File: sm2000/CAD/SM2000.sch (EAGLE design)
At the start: 228 parts, among them CN1 HDR100-3, CN10 ST-3509, CN11 HDR100-3, CN2 JS-MU3-002, CN3 DS-0518, CN5 ST-3509, CN8 ST-3509, J1 JMP-2PIN, J2 JMP-2PIN, J3 JMP-2PIN, J4 CONN-BOOM-XH-2A, P10 TPAD50, P11 TPAD50, P12 TPAD50, P13 TPAD50, P14 TPAD50, P16 TPAD50, P18 TPAD50, P19 TPAD50, P20 TPAD50, P21 TPAD50, P3 TPAD50, P4 TPAD50, P5 TPAD50, P6 TPAD50, P7 TPAD50, P8 TPAD50, P9 TPAD50, Q1 MMBT3904, Q2 MMBT3904, Q3 MMBT3904, Q4 MMBT3904, Q5 MMBT3904, Q6 MMBT3904, Q7 BC548, Q8 BC549, SW1 SW-LC2259, SW2 TS-026, SW3 SW-LC2259EENP, SW4 TS-026, SW5 TS-02B, U1 STM32F405VGT6, U10 DNL, U2 LD3985M33R, U3 STMPS2141, U4 EMIF02-USB03F2, U5 TPS54329E, U8 LM386M-1, U9 LMV341, X1 BU-SMA-H, X2 BU-SMA-H

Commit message: Continued edit of SM2000 .sch & .brd   RGB
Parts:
- removed R55: 0 Ohm, AA-ipc-7351-resistor:RESISTOR_0603
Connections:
- removed net !CPPT!: U1A.PD10
- removed net DAC1_OUT: R55.2
- removed net N$11: R55.1, U1A.PA4
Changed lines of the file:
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@@
 <part name="V124" library="A-SUPPLY2" deviceset="GND" device=""/>
 <part name="FB7" library="_RoweTel" deviceset="FB0805" device=""/>
-<part name="R55" library="AA-ipc-7351-resistor" deviceset="RESISTOR_" device="0603" value="0 Ohm"/>
 <part name="R54" library="AA-ipc-7351-resistor" deviceset="RESISTOR_" device="0603" value="0 Ohm"/>
 <part name="C55" library="AA-ipc-7351-capacitor" deviceset="CAPACITOR_" device="0402" value="1nF,25V,0402"/>
@@
 <instance part="V124" gate="GND" x="43.18" y="106.68"/>
 <instance part="FB7" gate="G$1" x="20.32" y="60.96"/>
-<instance part="R55" gate="G$1" x="83.82" y="208.28" smashed="yes" rot="R180">
-<attribute name="NAME" x="81.28" y="210.82" size="1.4224" layer="95" ratio="9"/>
-<attribute name="VALUE" x="86.36" y="210.82" size="1.4224" layer="96" ratio="9"/>
-</instance>
 <instance part="R54" gate="G$1" x="83.82" y="203.2" smashed="yes" rot="R180">
 <attribute name="NAME" x="81.788" y="204.978" size="1.4224" layer="95" ratio="9"/>
@@
 </segment>
 </net>
-<net name="!CPPT!" class="0">
-<segment>
-<pinref part="U1" gate="A" pin="PD10"/>
-<wire x1="147.32" y1="149.86" x2="165.1" y2="149.86" width="0.1524" layer="91"/>
-<label x="149.86" y="150.368" size="1.4224" layer="95" ratio="10"/>
-</segment>
-</net>
 <net name="!TEST!" class="0">
 <segment>
@@
 </segment>
 </net>
-<net name="DAC1_OUT" class="0">
-<segment>
-<pinref part="R55" gate="G$1" pin="2"/>
-<wire x1="78.74" y1="208.28" x2="66.04" y2="208.28" width="0.1524" layer="91"/>
-<label x="68.58" y="208.788" size="1.4224" layer="95" ratio="10"/>
-</segment>
-</net>
 <net name="DAC2_OUT" class="0">
 <segment>
@@
 </segment>
 </net>
-<net name="N$11" class="0">
-<segment>
-<pinref part="R55" gate="G$1" pin="1"/>
-<pinref part="U1" gate="A" pin="PA4"/>
-<wire x1="88.9" y1="208.28" x2="111.76" y2="208.28" width="0.1524" layer="91"/>
-</segment>
-</net>
 <net name="N$13" class="0">
 <segment>
@@
 <net name="N$90" class="0">
 <segment>
-<pinref part="C69" gate="G$1" pin="1"/>
-<wire x1="132.08" y1="215.9" x2="134.62" y2="215.9" width="0.1524" layer="91"/>
 <pinref part="C76" gate="G$1" pin="2"/>
-<wire x1="134.62" y1="215.9" x2="137.16" y2="215.9" width="0.1524" layer="91"/>
 <wire x1="134.62" y1="152.4" x2="137.16" y2="152.4" width="0.1524" layer="91"/>
-<wire x1="134.62" y1="215.9" x2="137.16" y2="215.9" width="0.1524" layer="91"/>
 <wire x1="137.16" y1="215.9" x2="137.16" y2="152.4" width="0.1524" layer="91"/>
 <pinref part="X2" gate="G$1" pin="1"/>
 <wire x1="144.78" y1="215.9" x2="137.16" y2="215.9" width="0.1524" layer="91"/>
+<pinref part="C69" gate="G$1" pin="1"/>
+<wire x1="137.16" y1="215.9" x2="134.62" y2="215.9" width="0.1524" layer="91"/>
+<wire x1="132.08" y1="215.9" x2="134.62" y2="215.9" width="0.1524" layer="91"/>
 <junction x="137.16" y="215.9"/>
 </segment>

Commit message: MERGE SCHEMATICS INTO sm2000.SCH AND UPDATE LIBRARY rgb
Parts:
- added C100, C93: 33p, rcl:C-EU025-024X044
- added C118, C121, C124, C125, C126, C129, C131, C91, C92, C97: 0.1u, rcl:C-EU025-024X044
- added C119: 10uF, _RoweTel:CAP-1210
- added C120: 39pF, rcl:C-EU025-024X044
- added C122, C89: 5p6, rcl:C-EU025-024X044
- added C123: 2-12pF, c-trimm:C-TRIMM3008
- added C127: 27pF, rcl:C-EU025-024X044
- added C128, C132: 150pF, rcl:C-EU025-024X044
- added C130, C133, C134, C88, C90, C96, C98: 1n, rcl:C-EU025-024X044
- added C87: 22pF, AA-ipc-7351-capacitor:CAPACITOR_0805
- added C94: 22p, rcl:C-EU025-024X044
- added C95: 1n DNL, rcl:C-EU025-024X044
- added C99: 47p, rcl:C-EU025-024X044
- added FB11, FB14, FB15, FB6: FB0805, _RoweTel:FB0805
- added L10: 168nH, rcl:L-US0204/5
- added L11, L13: RFC, inductor-neosid:Z14/40CCW
- added L12: 54nH, rcl:L-US0204/5
- added L14, L15: 57nH air core 4T 2mm ID, rcl:L-US0204/5
- added L20: 5.7uH +/- 10% Q>20, rcl:L-US0204/5
- added L21: 9.2uH +/- 10% Q>20, rcl:L-US0204/5
- added L22: 5.2uH +/- 10% Q>20, rcl:L-US0204/5
- added L23: 15uH +/- 10% Q>20, rcl:L-US0204/5
- added L9: 57nH, rcl:L-US0204/5
- added Q12: BRF92, transistor:-NPN-SOT23-EBC
- added Q13: BFQ19, transistor:-NPN-SOT23-EBC
- added Q14: RD01MUS2, _RoweTel:RD01MUS2
- added Q17, Q18: MMT2904, transistor:-NPN-SOT23-EBC
- added R108, R60, R93: 3k, AA-ipc-7351-resistor:RESISTOR_0805
- added R109, R113, R94: 1k, AA-ipc-7351-resistor:RESISTOR_0805
- added R110, R96, R97: 10, AA-ipc-7351-resistor:RESISTOR_0805
- added R111: 33k, AA-ipc-7351-resistor:RESISTOR_0805
- added R112: 15k, AA-ipc-7351-resistor:RESISTOR_0805
- added R114, R95: 50, AA-ipc-7351-resistor:RESISTOR_0805
- added R115, R92: 150, AA-ipc-7351-resistor:RESISTOR_0805
- added R55: 10k, AA-ipc-7351-resistor:RESISTOR_0805
- added R98: 47 DNL, AA-ipc-7351-resistor:RESISTOR_0805
- added R99: 4k7, AA-ipc-7351-resistor:RESISTOR_0805
- added U$10, U$11: ECS-10.7-15B, _RoweTel:ECS-10.7-15B
- added U7: SA612A, _RoweTel:SA612A
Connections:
- new net N$11: C100.1, L14.2
- new net N$112: C87.2, L9.1
- new net N$113: C95.1, R98.1
- new net N$114: C96.1, FB11.1, R99.2
- new net N$115: C97.1, FB6.2, R99.1
- new net N$116: L13.1
- new net N$118: C93.1, C98.2, L15.1
- new net N$140: C118.1, Q17.C, R108.2, R110.2, R111.2
- new net N$141: C121.2, Q17.B, Q18.C, R108.1
- new net N$142: C119.1, FB14.1, R110.1
- new net N$143: C120.1, L20.2, U$11.1
- new net N$144: C122.1, U$10.2, U$11.2
- new net N$145: C121.1, C123.E, L21.2, U$10.1
- new net N$146: C124.1, Q18.B, R111.1, R112.2
- new net N$147: C125.1, Q18.E, R113.2
- new net N$148: C126.1, Q17.E, R109.2
- new net N$149: C126.2, C127.1, C128.2, R114.2
- new net N$150: C128.1, C129.2, L22.2, U7.IN_B
- new net N$151: C127.2, L22.1, U7.IN_A
- new net N$152: FB15.2, R115.2
- new net N$153: C130.2, C131.2, R115.1, U7.VIN
- new net N$154: C132.2, U7.OSC_B
- new net N$155: C132.1
- new net N$156: C133.2, L23.1, U7.OUT_A
- new net N$157: C134.2, L23.2
- new net N$32: C98.1, L11.1, Q14.D
- new net N$33: C94.1, FB11.2, Q14.G, R98.2
- new net N$70: C88.1, Q12.E, R92.2
- new net N$71: C90.1, Q13.E, R95.2
- new net N$73: C91.1, L10.1, R55.2, R96.2
- new net N$74: C92.1, L12.1, R93.2, R96.1, R97.2
- new net N$75: C89.1, Q13.B, R93.1, R94.2
- new net N$78: C87.1, Q12.B, R55.1, R60.2
- new net N$79: L11.2, L13.2, R97.1
- new net N$82: C89.2, L10.2, Q12.C
- new net N$84: C94.2, L12.2, Q13.C
- new net N$9: C99.1, L14.1, L15.2
- new net VGG: FB6.1
- net +12V: now also FB14.2, FB15.1
- net GND: now also C100.2, C118.2, C119.2, C120.2, C122.2, C123.A, C129.1, C131.1, C133.1, C134.1, C88.2, C90.2, C91.2, C92.2, C93.2, C95.2, C96.2, C97.2, C99.2, L21.1, L9.2, Q14.S, R109.1, R113.1, R114.1, R60.1, R92.1, R94.1, R95.1, U7.GND
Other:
- note added: "+9V"
- note added: "1.4V"
- note added: "1.7V"
- note added: "2.4V"
- note added: "33p, 47p, 33p cap nets must be zero length"
- note added: "3T 6.25mm"
- note added: "6T 6.25mm"
- note added: "BASEBAND_AMP"
- note added: "Baseand AMP"
- note added: "DRIVER_PA"
- note added: "From TIA"
- note added: "Load/Adjust if PA stability is a problem"
- note added: "Mount Ls at right angles"
- note added: "No junction here!"
- note added: "TERMINATION INSENSATIVE AMPLIFIEER"
- note added: "TX 2ND LO"
- note added: "TX DAC"
- note added: "Vgg from uC DAC"
- note added: "XTAL 2ND MIXER"
- note added: "Z=1500"
- note added: "Z=3000"
- note added: "Z=50"
- note added: "from BPF/switch"
- note added: "to T/R switch"
- moved on the sheet: C28, C67, C68, C69, C71, C72, C73, C74, C75, C76, C77, C78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

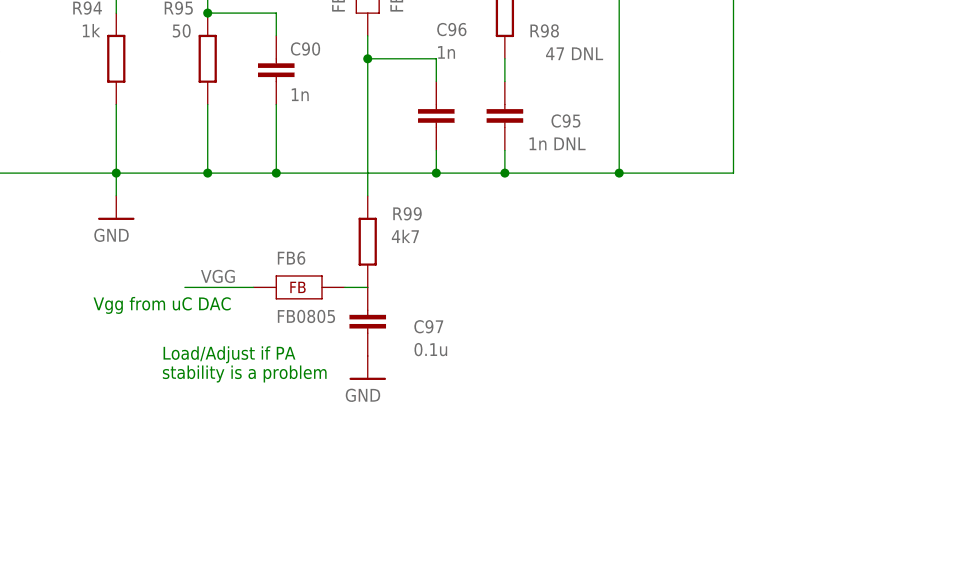
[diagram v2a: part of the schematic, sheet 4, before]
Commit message: test tweak by DR to sm2000.sch
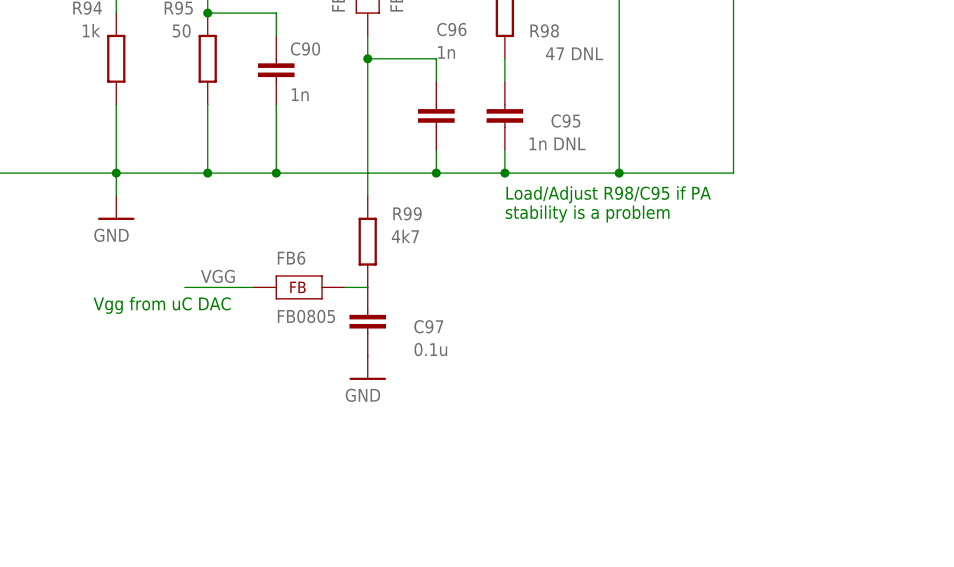
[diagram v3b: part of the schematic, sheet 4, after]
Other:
- note added: "Load/Adjust R98/C95 if PA stability is a problem"
- note removed: "Load/Adjust if PA stability is a problem"
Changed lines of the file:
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@@
 <?xml version="1.0" encoding="utf-8"?>
 <!DOCTYPE eagle SYSTEM "eagle.dtd">
-<eagle version="6.5.0">
+<eagle version="7.2.0">
 <drawing>
 <settings>
@@
 <setting verticaltext="up"/>
 </settings>
-<grid distance="0.1" unitdist="inch" unit="inch" style="lines" multiple="1" display="yes" altdistance="0.01" altunitdist="inch" altunit="inch"/>
+<grid distance="0.1" unitdist="inch" unit="inch" style="lines" multiple="1" display="no" altdistance="0.01" altunitdist="inch" altunit="inch"/>
 <layers>
 <layer number="1" name="Top" color="4" fill="1" visible="no" active="no"/>
@@
 <text x="88.9" y="43.18" size="1.4224" layer="91">Vgg from uC DAC</text>
 <text x="160.02" y="121.92" size="1.4224" layer="91">+9V</text>
-<text x="96.52" y="35.56" size="1.4224" layer="91">Load/Adjust if PA
+<text x="134.62" y="53.34" size="1.4224" layer="91">Load/Adjust R98/C95 if PA
 stability is a problem</text>
 <text x="33.02" y="88.9" size="1.4224" layer="91" rot="R180">from BPF/switch</text>

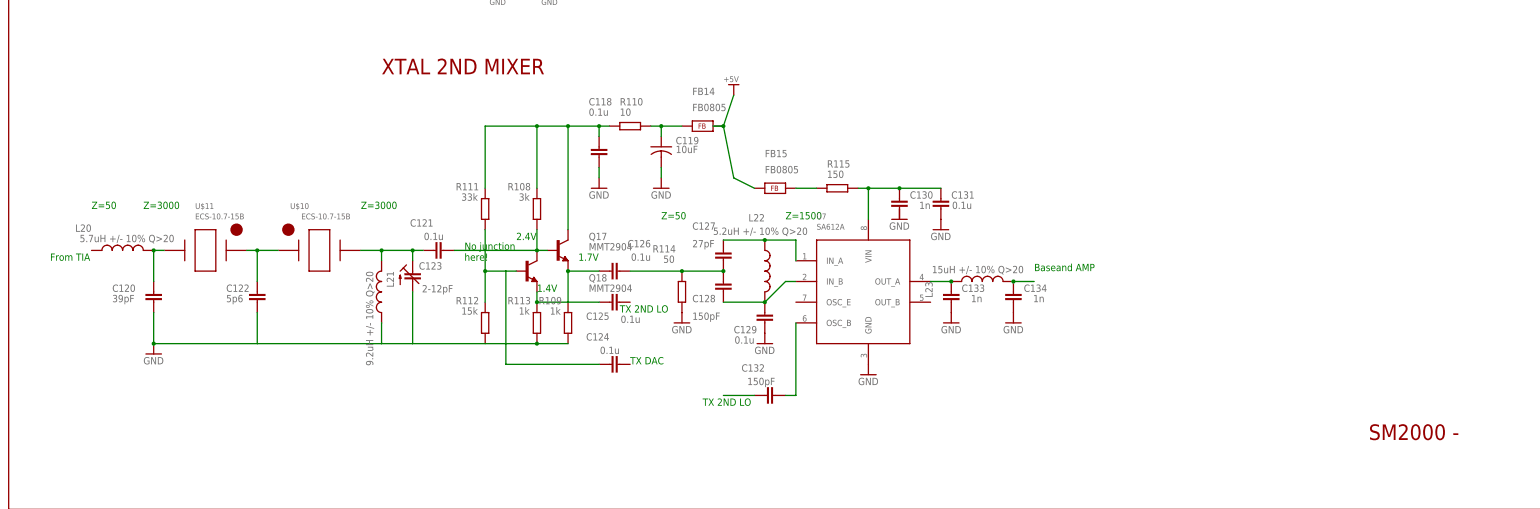
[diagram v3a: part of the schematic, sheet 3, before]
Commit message: INTEGRATED 1ST MIXER BPF SWITCH INTO SM2000.SCH. CORRECTED CENTERING ON SOME COMPONENTS IN ROWETEL.LBR SHORTENED LEADS ON FB0805 SYMBOL. RGB
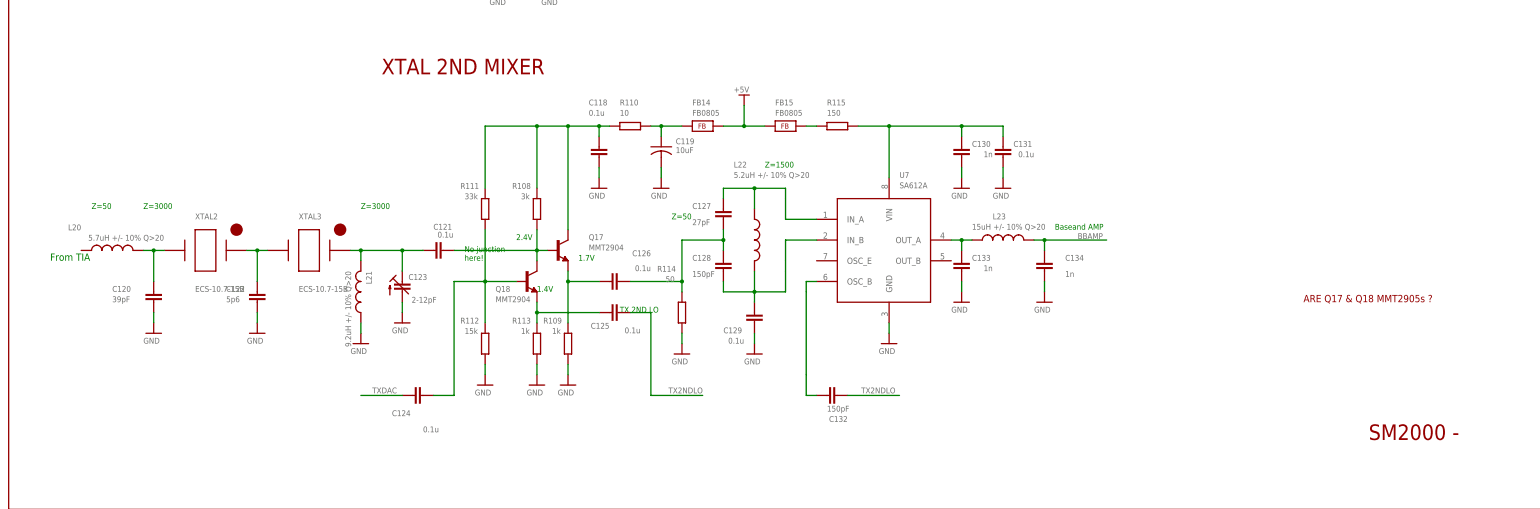
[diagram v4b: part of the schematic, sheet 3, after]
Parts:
- removed U$10: ECS-10.7-15B, _RoweTel:ECS-10.7-15B
- added C110, C113, C138, C141: 12p, AA-ipc-7351-capacitor:CAPACITOR_0805
- added C111, C112, C139, C140: 3p3, AA-ipc-7351-capacitor:CAPACITOR_0805
- added C114, C142: 0.5p, AA-ipc-7351-capacitor:CAPACITOR_0805
- added C115, C116, C117, C135, C137, C147, C148, C149: 1n, AA-ipc-7351-capacitor:CAPACITOR_0805
- added C136: 1u, _RoweTel:CAP-TANT-1206
- added C143, C144: 2p2, AA-ipc-7351-capacitor:CAPACITOR_0805
- added C145, C146: 22p, AA-ipc-7351-capacitor:CAPACITOR_0805
- added D10, D11, D12, D13: BAR64-02V, _RoweTel:BAR64-02V
- added FB17, FB18, FB19, FB20, FB21: FB0805, _RoweTel:FB0805
- added L16, L17, L18, L19: 68nH 4.5T 5mm ID, rcl:L-US0204/5
- added L24: 260nH 8T 6.25mm ID, rcl:L-US0204/5
- added L25: 53nH 3T 5mm ID, rcl:L-US0204/5
- added L26: 220nH 7T 6.25mm ID, rcl:L-US0204/5
- added R45, R47: 18k, _RoweTel:RES0805
- added R48: 68k, _RoweTel:RES0805
- added R49: 2k2, _RoweTel:RES0805
- added U12: PGA-103+, _RoweTel:PGA-103+
- added U13: ADE-1, _RoweTel:ADE-1
- added XTAL3: ECS-10.7-15B, _RoweTel:ECS-10.7-15B
- renumbered U$11 to XTAL2
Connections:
- net N$157 renamed BBAMP
- new net N$125: C110.1, C111.1, C114.2, L16.1
- new net N$126: C112.2, C113.2, C114.1, L17.1
- new net N$127: C111.2, U13.RF
- new net N$128: C116.1, FB19.2, R45.2
- new net N$129: C115.1, FB18.1, R47.2
- new net N$130: C117.1, D10.A, FB19.1
- new net N$131: C117.2, FB20.1, U12.OUT
- new net N$132: C135.1, C136.1, FB20.2, FB21.1
- new net N$133: FB21.2
- new net N$134: C137.1, D11.A, FB18.2
- new net N$135: C112.1, D10.C, D11.C, FB17.2
- new net N$136: C138.1, C139.1, C142.2, L18.1
- new net N$137: C140.2, C141.2, C142.1, L19.1
- new net N$138: C139.2
- new net N$139: C143.1, C144.2, L24.1
- new net N$149: C140.1, C145.1, D12.A, L25.1
- new net N$157: C149.1, D13.A, L26.2
- new net N$158: C148.1, L26.1, R49.1
- new net N$50: U7.IN_B
- new net N$51: C128.1, C129.2, L22.2
- new net TX2NDLO: C125.2, C132.1
- new net TXDAC: C124.2
- net GND: now also C110.2, C113.1, C115.2, C116.2, C130.1, C135.2, C136.2, C138.2, C141.1, C145.2, C146.2, C148.2, D12.C, FB17.1, L16.2, L17.2, L18.2, L19.2, L24.2, R112.1, R48.1, U12.GND, U12.GND1
- net N$144: now also XTAL3.1; no longer U$10.2
- net N$145: now also XTAL3.2; no longer U$10.1
- net N$150: now also C146.1, C147.2, D13.C, L25.2; no longer C128.1, C129.2, L22.2, U7.IN_B
- net N$155: now also C147.1, R48.2; no longer C132.1
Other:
- note added: "+12V TX 0V RX"
- note added: "+12V for RX"
- note added: "+3v3 60mA"
- note added: "12V for TX"
- note added: "1ST_MIXER_BPF_SWITCH"
- note added: "1st LO"
- note added: "ARE Q17 & Q18 MMT2905s ?"
- note added: "Alternate load: Same PCB layout 0.4dB IL Poorer attn"
- note added: "Antenna SMA"
- note added: "Driver/PA input"
- note added: "L1 and L2 at right angles with shield"
- note added: "L8 and L9 at right angles with shield"
- note added: "PA Output"
- note added: "Tune L1 and L2 to 146MHz"
- note added: "Tune L4 to 146MHz"
- note added: "Tune L8 and L9 to 146MHz"
- note added: "to TIA"
- note removed: "TX DAC"
- moved on the sheet: C123, C124, C125, C126, C127, C128, C129, C130, C131, C132, C133, C134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
